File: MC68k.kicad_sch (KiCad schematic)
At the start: 3 parts, among them U14 MC68HC000FN20

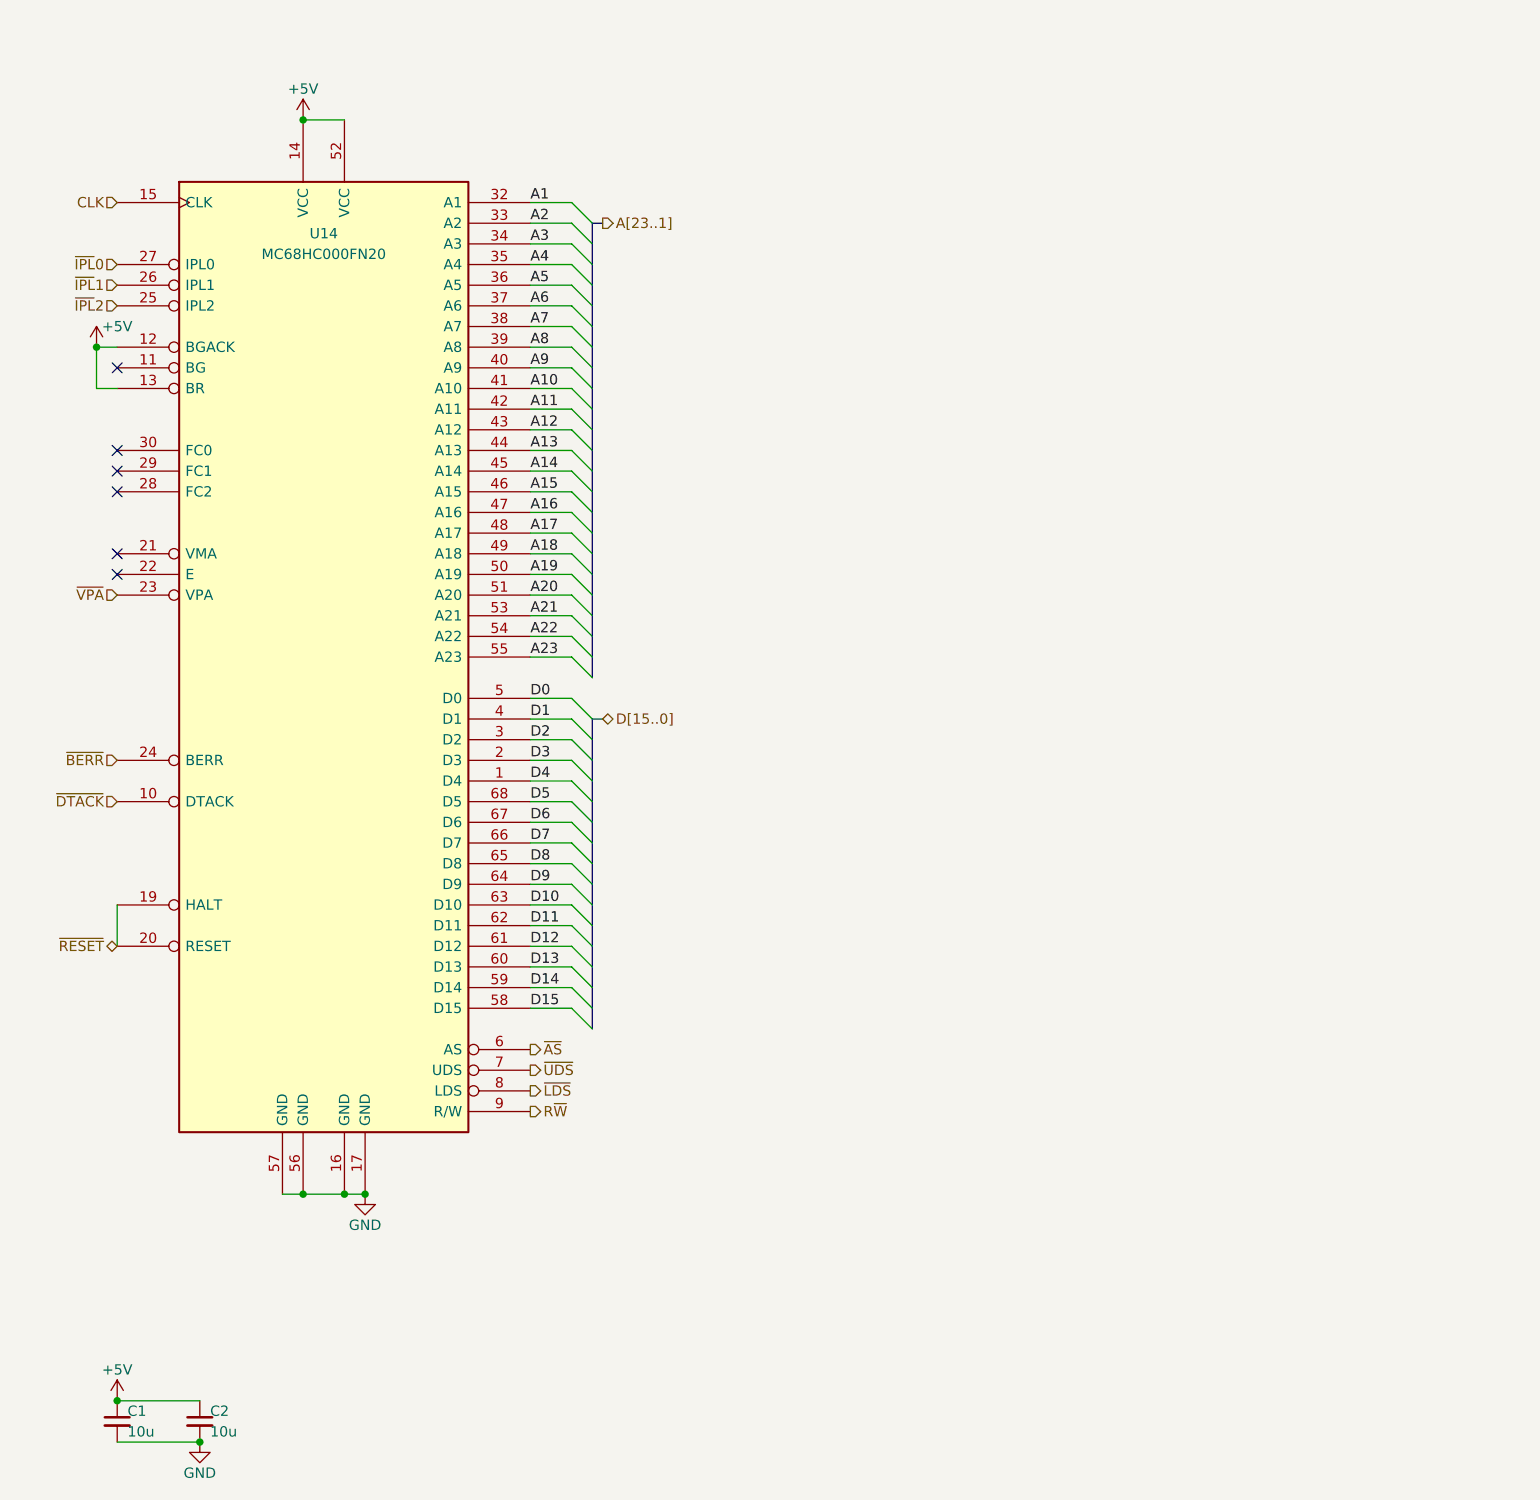
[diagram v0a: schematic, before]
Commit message: Switch to '030
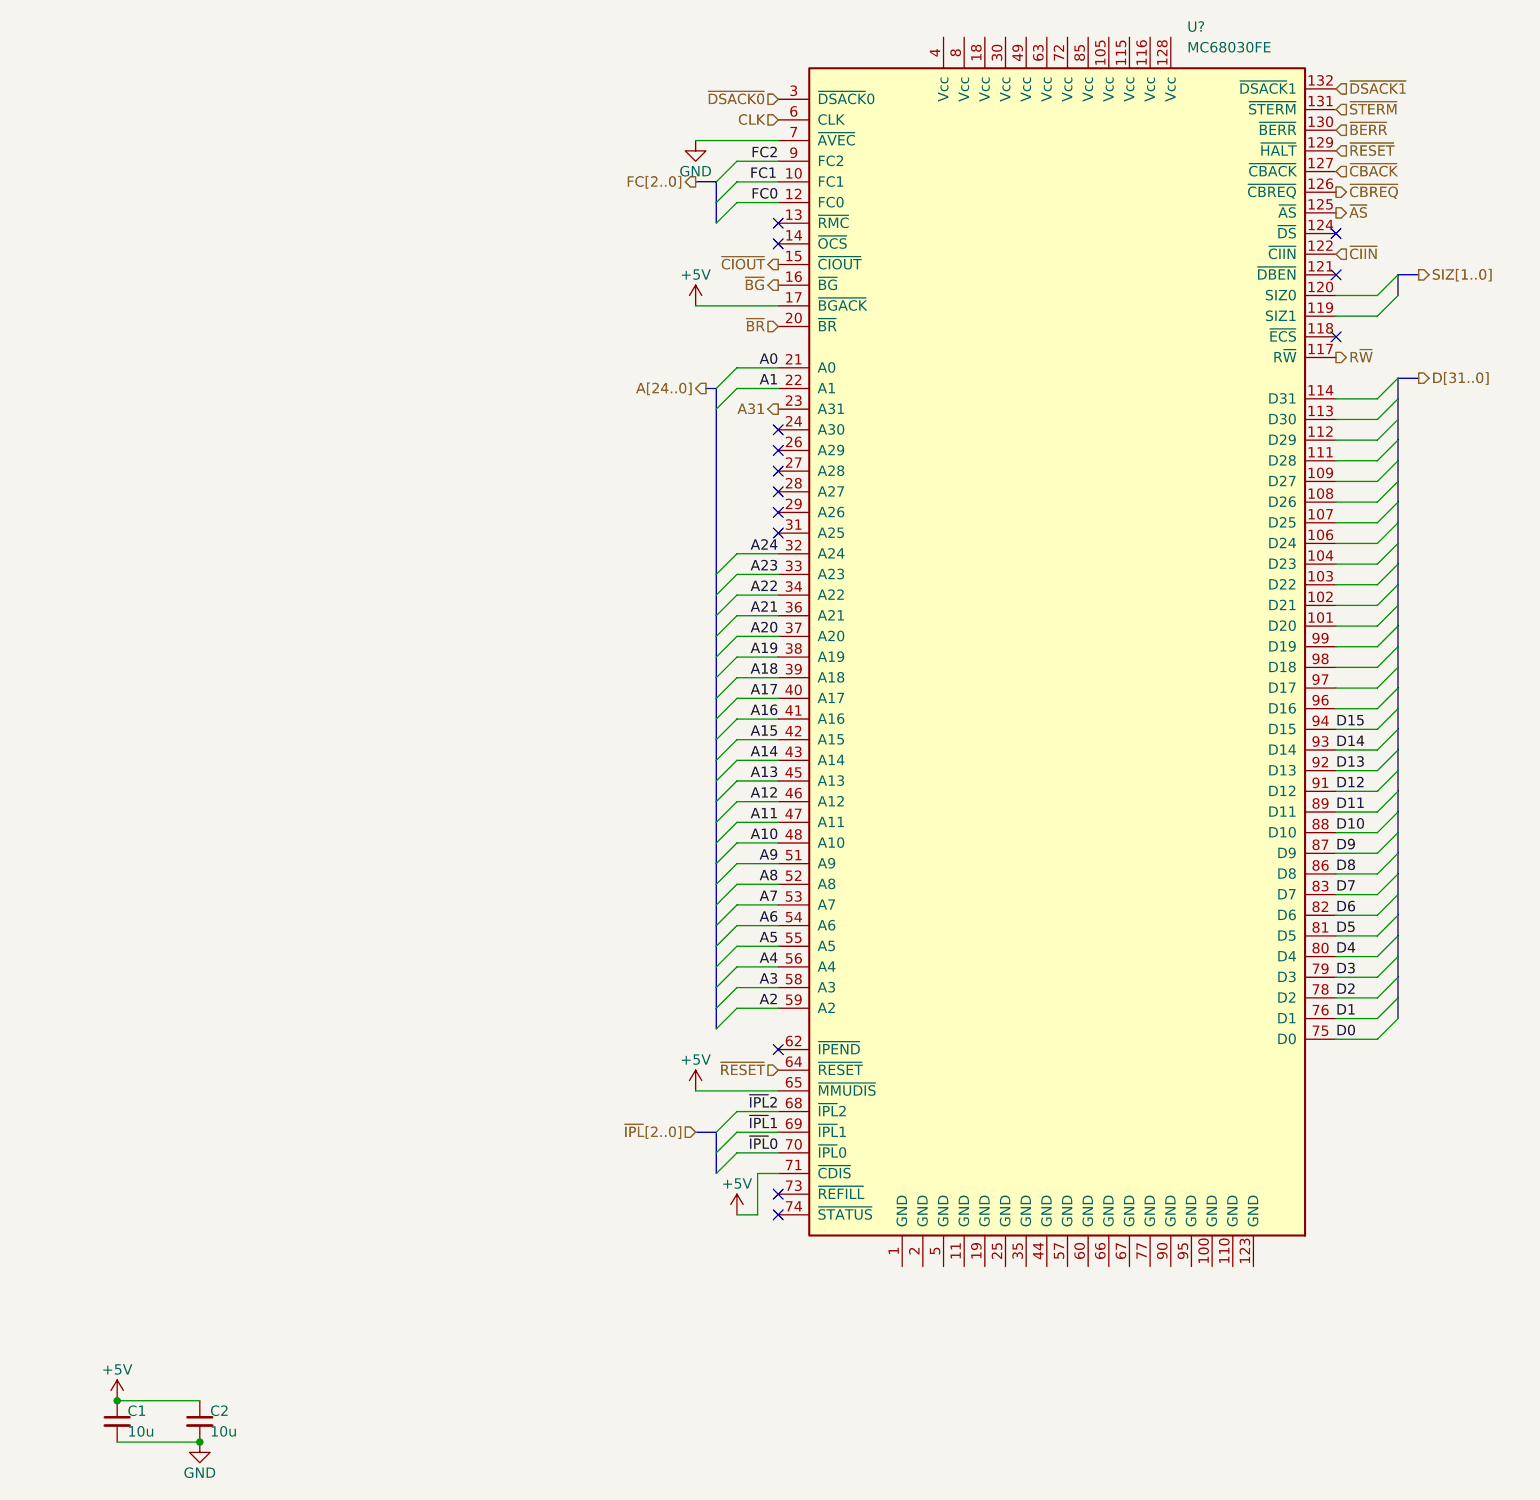
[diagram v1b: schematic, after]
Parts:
- removed U14: MC68HC000FN20, stdpads:PLCC-68, symbol CPU_NXP_68000:MC68000FN
- added U?: MC68030FE, stdpads:Motorola_CQFP-132, symbol GW_CPU:MC68030FE
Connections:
- net +5V: now also U?.17 (~{BGACK}), U?.65 (~{MMUDIS}), U?.71 (~{CDIS})
- net A1: now also U?.22 (A1)
- net A10: now also U?.48 (A10)
- net A11: now also U?.47 (A11)
- net A12: now also U?.46 (A12)
- net A13: now also U?.45 (A13)
- net A14: now also U?.43 (A14)
- net A15: now also U?.42 (A15)
- net A16: now also U?.41 (A16)
- net A17: now also U?.40 (A17)
- net A18: now also U?.39 (A18)
- net A19: now also U?.38 (A19)
- net A2: now also U?.59 (A2)
- net A20: now also U?.37 (A20)
- net A21: now also U?.36 (A21)
- net A22: now also U?.34 (A22)
- net A23: now also U?.33 (A23)
- net A3: now also U?.58 (A3)
- net A4: now also U?.56 (A4)
- net A5: now also U?.55 (A5)
- net A6: now also U?.54 (A6)
- net A7: now also U?.53 (A7)
- net A8: now also U?.52 (A8)
- net A9: now also U?.51 (A9)
- net CLK: now also U?.6 (CLK)
- net D0: now also U?.75 (D0)
- net D1: now also U?.76 (D1)
- net D10: now also U?.88 (D10)
- net D11: now also U?.89 (D11)
- net D12: now also U?.91 (D12)
- net D13: now also U?.92 (D13)
- net D14: now also U?.93 (D14)
- net D15: now also U?.94 (D15)
- net D2: now also U?.78 (D2)
- net D3: now also U?.79 (D3)
- net D4: now also U?.80 (D4)
- net D5: now also U?.81 (D5)
- net D6: now also U?.82 (D6)
- net D7: now also U?.83 (D7)
- net D8: now also U?.86 (D8)
- net D9: now also U?.87 (D9)
- net GND: now also U?.7 (~{AVEC})
- net R~{W}: now also U?.117 (R~{W})
- net ~{AS}: now also U?.125 (~{AS})
- net ~{BERR}: now also U?.130 (~{BERR})
- net ~{IPL}0: now also U?.70 (~{IPL}0)
- net ~{IPL}1: now also U?.69 (~{IPL}1)
- net ~{IPL}2: now also U?.68 (~{IPL}2)
- net ~{RESET}: now also U?.129 (~{HALT}), U?.64 (~{RESET})
- new net A0: U?.21 (A0)
- new net A24: U?.32 (A24)
- new net A31: U?.23 (A31)
- new net FC0: U?.12 (FC0)
- new net FC1: U?.10 (FC1)
- new net FC2: U?.9 (FC2)
- new net ~{BG}: U?.16 (~{BG})
- new net ~{BR}: U?.20 (~{BR})
- new net ~{CBACK}: U?.127 (~{CBACK})
- new net ~{CBREQ}: U?.126 (~{CBREQ})
- new net ~{CIIN}: U?.122 (~{CIIN})
- new net ~{CIOUT}: U?.15 (~{CIOUT})
- new net ~{DSACK0}: U?.3 (~{DSACK}0)
- new net ~{DSACK1}: U?.132 (~{DSACK}1)
- new net ~{STERM}: U?.131 (~{STERM})
- no-connect marks 6 -> 14
